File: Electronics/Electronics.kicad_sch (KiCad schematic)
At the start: 0 parts

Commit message: power + usb
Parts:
- added BT1, BT2: 4xAA, symbol Device:Battery
- added C29, C44, C46: 22uF, symbol Device:C_Polarized
- added C43, C45: C, symbol Device:C
- added D6, D7: D, symbol Device:D
- added P1: USB_C_Plug_USB2.0, symbol Connector:USB_C_Plug_USB2.0
- added R18, R19, R21: 1k, symbol Device:R
- added SW5: SW_DIP_x02, symbol Switch:SW_DIP_x02
- added U10: ~, Package_DFN_QFN:QFN-16-1EP_3x3mm_P0.5mm_EP1.7x1.7mm, symbol FSUSB74:FSUSB74
- added U11, U12: AMS1117-3.3, Package_TO_SOT_SMD:SOT-223-3_TabPin2, symbol Regulator_Linear:AMS1117-3.3
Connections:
- new net: BT1.2 (-), C43.2, C44.2, C45.2, C46.2, U12.1 (GND)
- new net: R19.1, SW5.3, U10.6 (SEL0)
- new net: R21.1, U10.15 (/OE)
- new net: R18.1, SW5.4, U10.5 (SEL1)
- new net: D6.1 (K), P1.A4 (VBUS), P1.A9 (VBUS), P1.B4 (VBUS), P1.B9 (VBUS), U11.3 (VI)
- new net: BT1.1 (+), BT2.2 (-)
- new net D+: P1.A6 (D+), U10.2 (D+)
- new net D-: P1.A7 (D-), U10.3 (D-)
- new net GND: C29.2, P1.A1 (GND), P1.A12 (GND), P1.B1 (GND), P1.B12 (GND), P1.S1 (SHIELD), R18.2, R19.2, R21.2, U10.1 (GND), U11.1 (GND)
- new net Gyro Controller/USB+: U10.13 (HSD0+)
- new net Gyro Controller/USB-: U10.14 (HSD0-)
- new net Motor Controller/USB+: U10.11 (HSD1+)
- new net Motor Controller/USB-: U10.12 (HSD1-)
- new net VBAT: BT2.1 (+), C43.1, C44.1, D7.1 (K), U12.3 (VI)
- new net VCC: C29.1, C45.1, C46.1, D6.2 (A), D7.2 (A), SW5.1, SW5.2, U10.4 (VCC), U11.2 (VO), U12.2 (VO)
- no-connect marks 0 -> 4
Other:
- sheet Gyro Controller ports: added READY, SCL, SDA, USB+, USB-; removed none
- sheet Motor Controller ports: added ML_A1, ML_A2, ML_B1, ML_B2, MR_A1, MR_A2, MR_B1, MR_B2, READY, SCL, SDA, USB+, USB-, VBAT; removed none

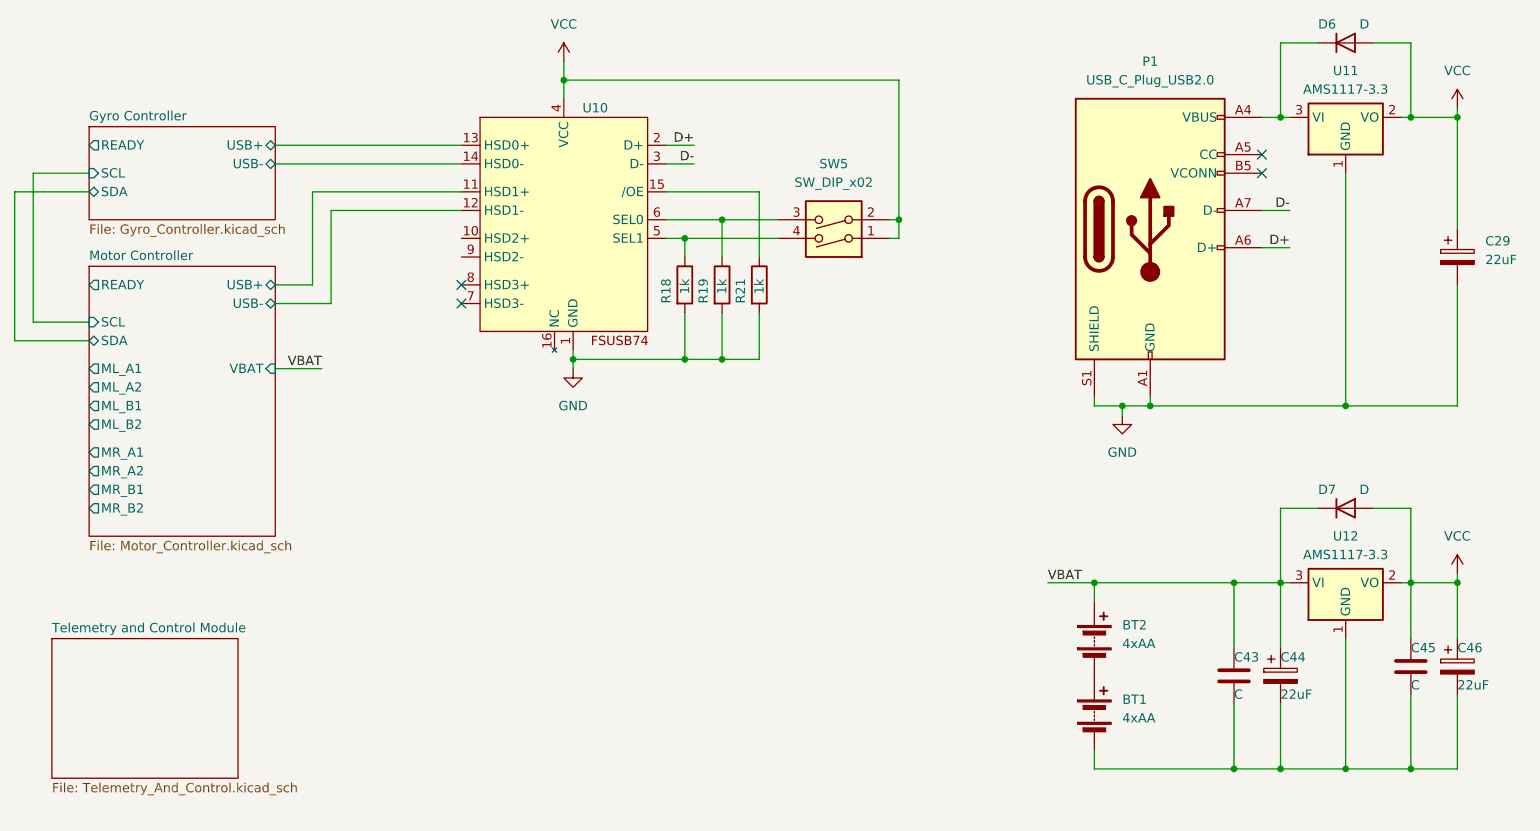
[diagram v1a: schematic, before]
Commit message: USB to UART converter
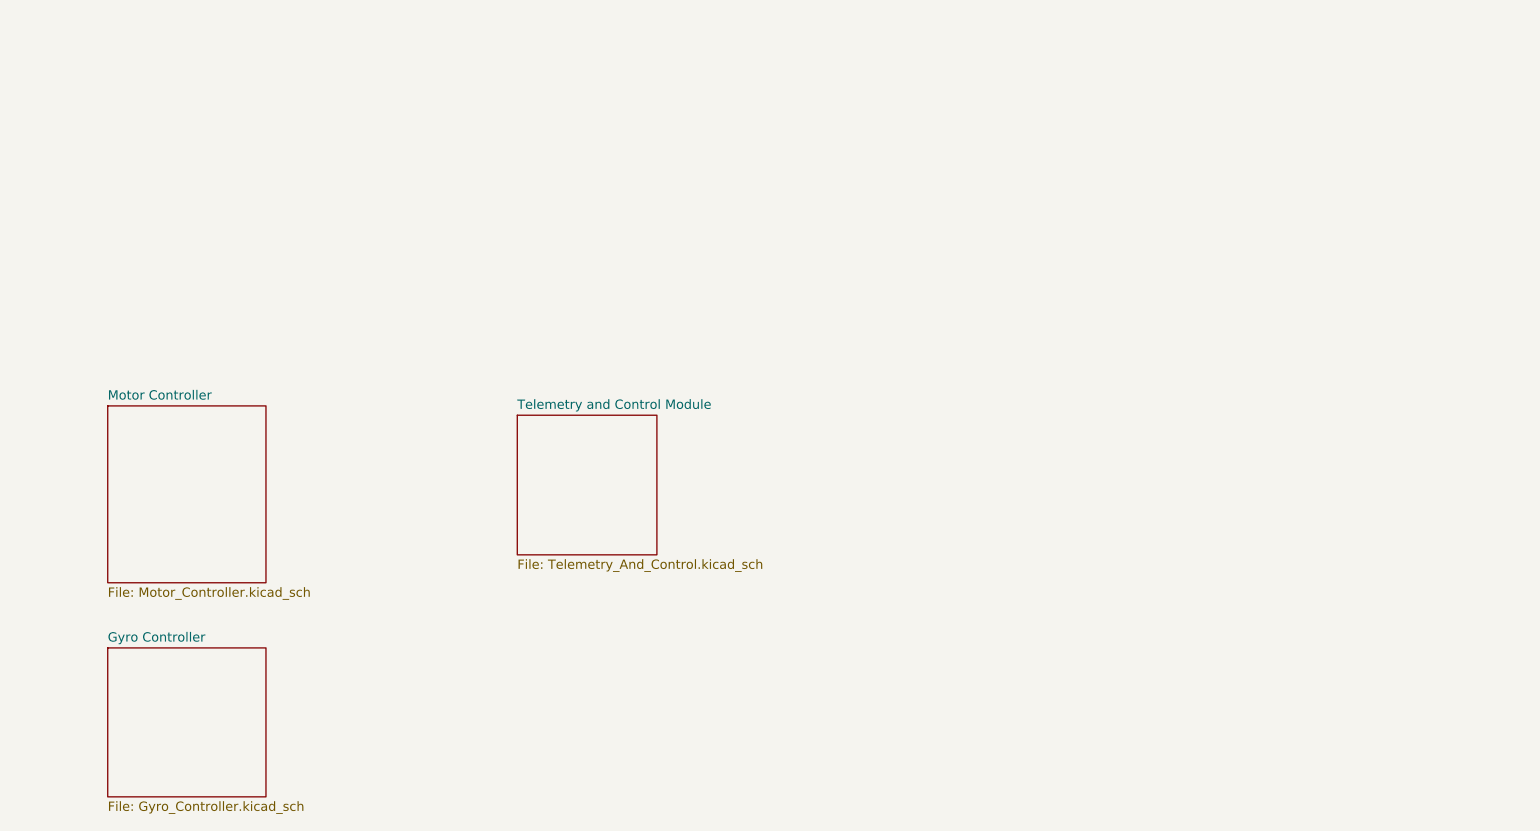
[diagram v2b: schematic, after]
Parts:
- removed BT1, BT2: 4xAA, symbol Device:Battery
- removed C29, C44, C46: 22uF, symbol Device:C_Polarized
- removed C43, C45: C, symbol Device:C
- removed D6, D7: D, symbol Device:D
- removed P1: USB_C_Plug_USB2.0, symbol Connector:USB_C_Plug_USB2.0
- removed R18, R19, R21: 1k, symbol Device:R
- removed SW5: SW_DIP_x02, symbol Switch:SW_DIP_x02
- removed U10: ~, Package_DFN_QFN:QFN-16-1EP_3x3mm_P0.5mm_EP1.7x1.7mm, symbol FSUSB74:FSUSB74
- removed U11, U12: AMS1117-3.3, Package_TO_SOT_SMD:SOT-223-3_TabPin2, symbol Regulator_Linear:AMS1117-3.3
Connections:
- no-connect marks 4 -> 0
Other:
- sheet Gyro Controller ports: added none; removed READY, SCL, SDA, USB+, USB-
- sheet Motor Controller ports: added none; removed ML_A1, ML_A2, ML_B1, ML_B2, MR_A1, MR_A2, MR_B1, MR_B2, READY, SCL, SDA, USB+, USB-, VBAT
